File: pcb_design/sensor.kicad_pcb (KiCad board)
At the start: 2 copper layers, 26 x 23 mm, 10 parts, among them P1 CONN_02X03, P2 CONN_01X03, U1 AS5311

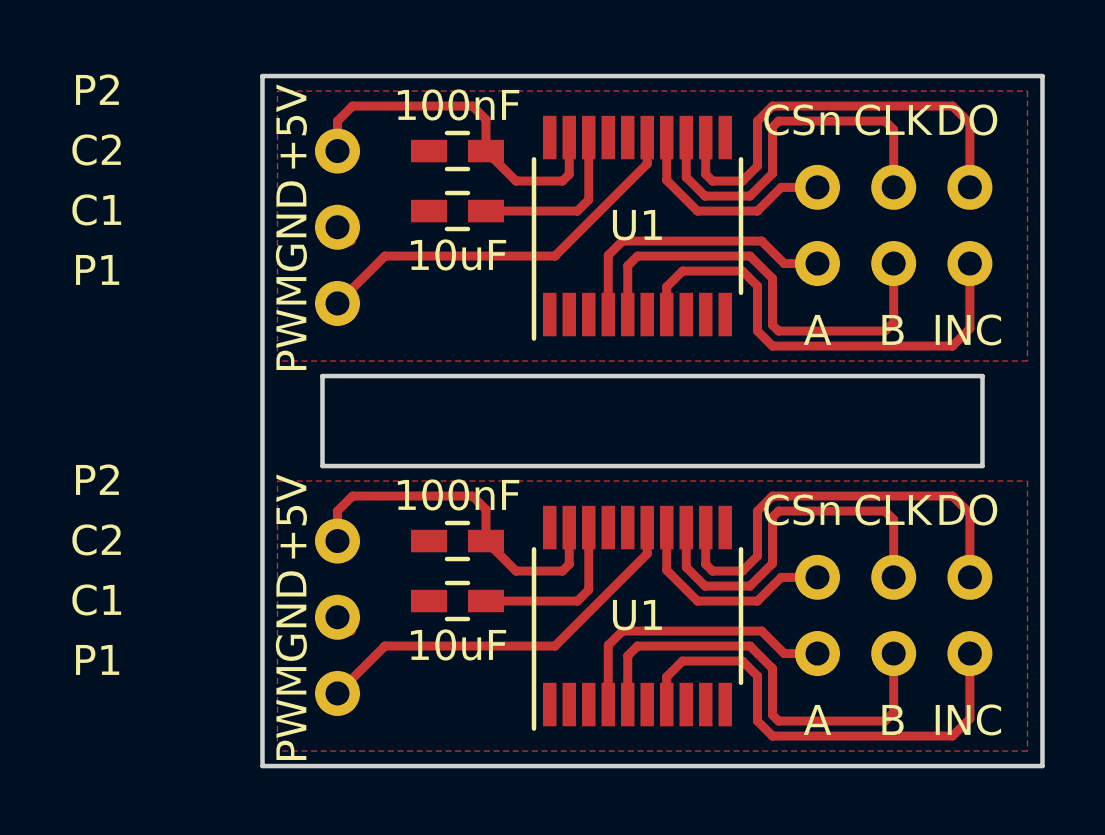
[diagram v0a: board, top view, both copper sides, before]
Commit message: - More progress on the DRO WebApp - Repository cleanup - Added GPL (for webapp) and CC-BY-SA-4.0 (pcb design) licences
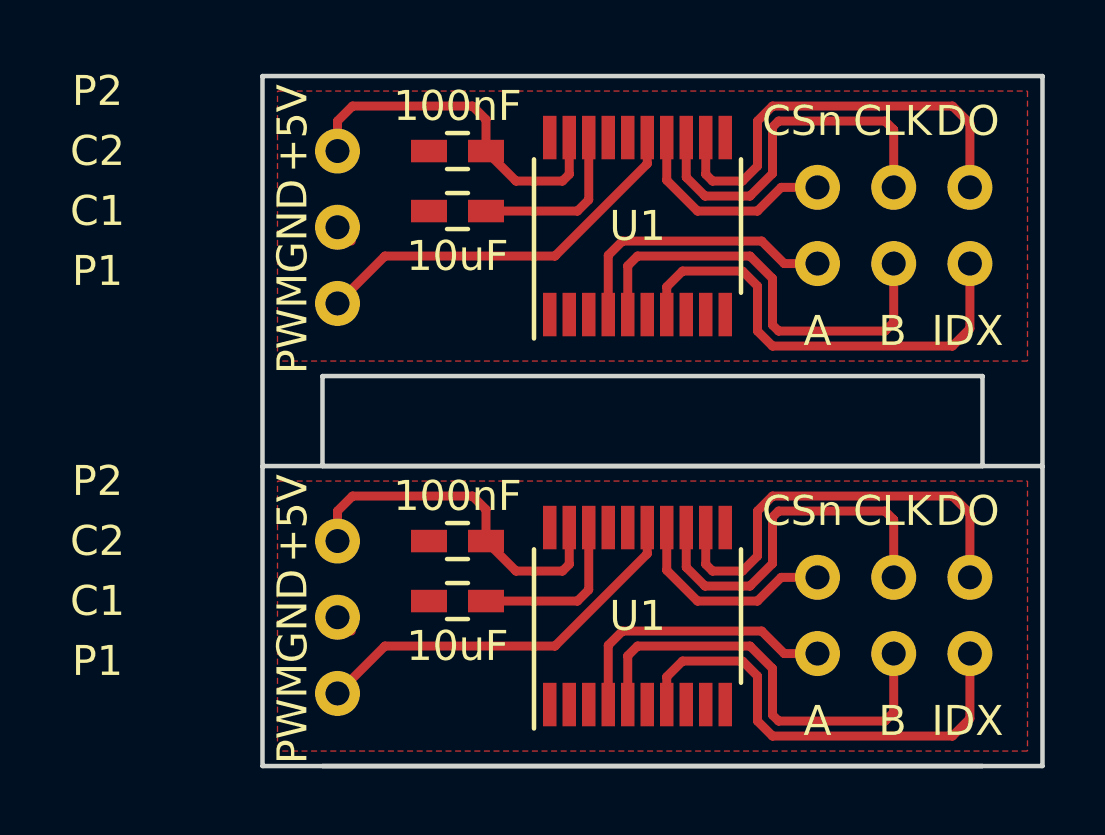
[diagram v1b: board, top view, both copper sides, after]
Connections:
- net /INC renamed /IDX
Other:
- outline, holes or cut-outs redrawn
- board text added: "IDX"
- board text removed: "INC"
